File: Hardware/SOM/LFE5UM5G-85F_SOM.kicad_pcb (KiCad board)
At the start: 2 copper layers, 67.6 x 25.4 mm, 17 parts, among them J1 SODIMM-200_Split, U1 LFE5UM5G-85F-8BG381x, U2 AS4C256M16D3

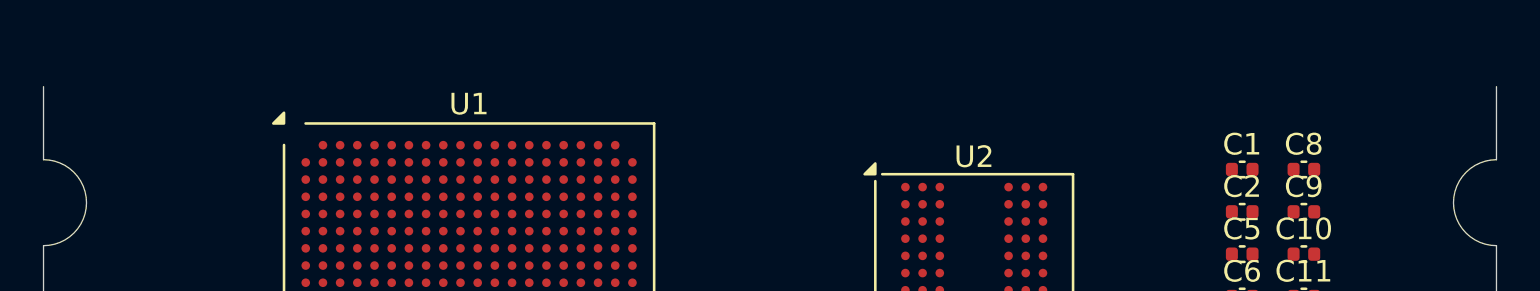
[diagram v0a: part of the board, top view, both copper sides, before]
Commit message: SOM board outline
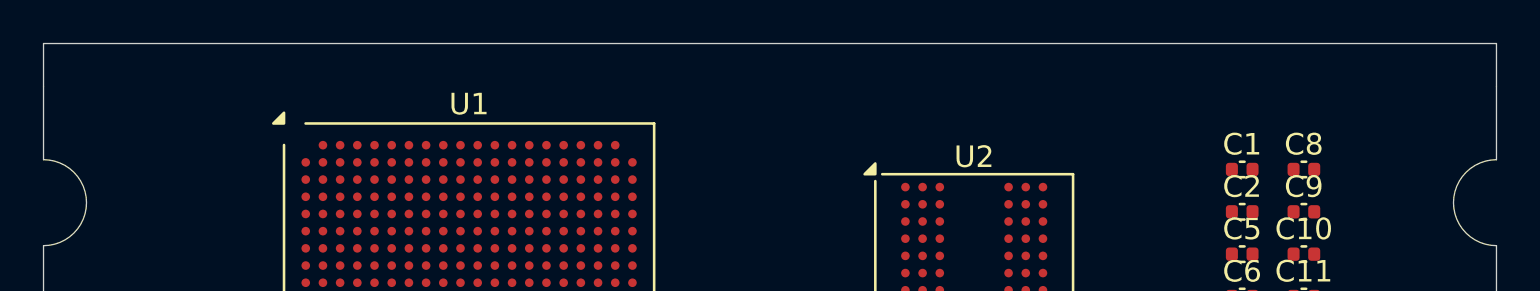
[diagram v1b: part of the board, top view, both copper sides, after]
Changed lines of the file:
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@@
+		)
+	)
+	(gr_line
+		(start 51.45 51.625)
+		(end 51.45 49.62)
+		(stroke
+			(width 0.05)
+			(type default)
+		)
+		(layer "Edge.Cuts")
+	)
+	(gr_line
+		(start 119.05 49.62)
+		(end 51.45 49.62)
+		(stroke
+			(width 0.05)
+			(type default)
+		)
+		(layer "Edge.Cuts")
+	)
+	(gr_line
+		(start 119.05 51.625)
+		(end 119.05 49.62)
+		(stroke
+			(width 0.05)
+			(type default)
+		)
+		(layer "Edge.Cuts")
+	)
+	(dimension
+		(type orthogonal)
+		(layer "F.Cu")
+		(pts
+			(xy 50.95 49.62) (xy 50.95 77.53)
+		)
+		(height -9.15)
+		(orientation 1)
+		(format
+			(prefix "")
+			(suffix "")
+			(units 3)
+			(units_format 1)
+			(precision 4)
+		)
+		(style
+			(thickness 0.2)
+			(arrow_length 1.27)
+			(text_position_mode 0)
+			(arrow_direction outward)
+			(extension_height 0.58642)
+			(extension_offset 0.5)
+			(keep_text_aligned yes)
+		)
+		(gr_text "27,9100 mm"
+			(at 40 63.575 90)
+			(layer "F.Cu")
+			(effects
+				(font
+					(size 1.5 1.5)
+					(thickness 0.3)
+				)
+			)
 		)
 	)

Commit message: BB SOM connector
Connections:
- J1 pad 2: unconnected-(J1-Pad2) -> ANY
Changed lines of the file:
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@@
 	(net 52 "unconnected-(J1-Pad55)")
 	(net 53 "unconnected-(J1-Pad152)")
-	(net 54 "unconnected-(J1-Pad2)")
+	(net 54 "ANY")
 	(net 55 "unconnected-(J1-Pad42)")
 	(net 56 "unconnected-(J1-Pad94)")
@@
 		)
 		(sheetname "/DDR/")
-		(sheetfile "ddr.kicad_sch")
+		(sheetfile "DDR.kicad_sch")
 		(attr smd)
 		(fp_line
@@
 		(property ki_fp_filters "Choke_* *Coil* Inductor_* L_*")
 		(sheetname "/DDR/")
-		(sheetfile "ddr.kicad_sch")
+		(sheetfile "DDR.kicad_sch")
 		(attr smd)
 		(fp_line
@@
 		)
 		(property ki_fp_filters "*SODIMM*")
-		(sheetname "/Connector/")
-		(sheetfile "connector.kicad_sch")
-		(attr exclude_from_pos_files allow_soldermask_bridges)
+		(sheetname "/SOM Connector/")
+		(sheetfile "Connector.kicad_sch")
+		(attr exclude_from_pos_files dnp allow_soldermask_bridges)
 		(fp_rect
 			(start -0.352 -1.302)
@@
 			(size 0.45 2.35)
 			(layers "B.Cu" "B.Mask")
-			(net 54 "unconnected-(J1-Pad2)")
+			(net 54 "ANY")
 			(pinfunction "2")
 			(pintype "passive")
@@
 		)
 		(sheetname "/DDR/")
-		(sheetfile "ddr.kicad_sch")
+		(sheetfile "DDR.kicad_sch")
 		(attr smd)
 		(fp_line
@@
 		)
 		(sheetname "/DDR/")
-		(sheetfile "ddr.kicad_sch")
+		(sheetfile "DDR.kicad_sch")
 		(attr smd)
 		(fp_line
@@
 		)
 		(sheetname "/DDR/")
-		(sheetfile "ddr.kicad_sch")
+		(sheetfile "DDR.kicad_sch")
 		(attr smd)
 		(fp_line
@@
 		)
 		(sheetname "/DDR/")
-		(sheetfile "ddr.kicad_sch")
+		(sheetfile "DDR.kicad_sch")
 		(attr smd)
 		(fp_line
@@
 		)
 		(sheetname "/DDR/")
-		(sheetfile "ddr.kicad_sch")
+		(sheetfile "DDR.kicad_sch")
 		(attr smd)
 		(fp_line
@@
 		)
 		(sheetname "/DDR/")
-		(sheetfile "ddr.kicad_sch")
+		(sheetfile "DDR.kicad_sch")
 		(attr smd)
 		(fp_line
@@
 		)
 		(sheetname "/DDR/")
-		(sheetfile "ddr.kicad_sch")
+		(sheetfile "DDR.kicad_sch")
 		(attr smd)
 		(fp_line
@@
 		(property ki_fp_filters "Lattice?caBGA*17x17mm*Layout20x20*P0.8mm*")
 		(sheetname "/FPGA/")
-		(sheetfile "io.kicad_sch")
+		(sheetfile "FPGA.kicad_sch")
 		(solder_mask_margin 0.075)
 		(attr smd)
@@
 		(property ki_fp_filters "Choke_* *Coil* Inductor_* L_*")
 		(sheetname "/DDR/")
-		(sheetfile "ddr.kicad_sch")
+		(sheetfile "DDR.kicad_sch")
 		(attr smd)
 		(fp_line
@@
 		)
 		(sheetname "/DDR/")
-		(sheetfile "ddr.kicad_sch")
+		(sheetfile "DDR.kicad_sch")
 		(attr smd)
 		(fp_line
@@
 		)
 		(sheetname "/DDR/")
-		(sheetfile "ddr.kicad_sch")
+		(sheetfile "DDR.kicad_sch")
 		(attr smd)
 		(fp_line
@@
 		)
 		(sheetname "/DDR/")
-		(sheetfile "ddr.kicad_sch")
+		(sheetfile "DDR.kicad_sch")
 		(attr smd)
 		(fp_line
@@
 		(property ki_fp_filters "BGA*9.0x13.0mm*P0.8mm*")
 		(sheetname "/DDR/")
-		(sheetfile "ddr.kicad_sch")
+		(sheetfile "DDR.kicad_sch")
 		(attr smd)
 		(fp_line
@@
 		)
 		(sheetname "/DDR/")
-		(sheetfile "ddr.kicad_sch")
+		(sheetfile "DDR.kicad_sch")
 		(attr smd)
 		(fp_line
@@
 		(layer "Edge.Cuts")
 	)
-	(dimension
-		(type orthogonal)
-		(layer "F.Cu")
-		(pts
-			(xy 50.95 49.62) (xy 50.95 77.53)
-		)
-		(height -9.15)
-		(orientation 1)
-		(format
-			(prefix "")
-			(suffix "")
-			(units 3)
-			(units_format 1)
-			(precision 4)
-		)
-		(style
-			(thickness 0.2)
-			(arrow_length 1.27)
-			(text_position_mode 0)
-			(arrow_direction outward)
-			(extension_height 0.58642)
-			(extension_offset 0.5)
-			(keep_text_aligned yes)
-		)
-		(gr_text "27,9100 mm"
-			(at 40 63.575 90)
-			(layer "F.Cu")
-			(effects
-				(font
-					(size 1.5 1.5)
-					(thickness 0.3)
-				)
-			)
-		)
-	)
 	(embedded_fonts no)

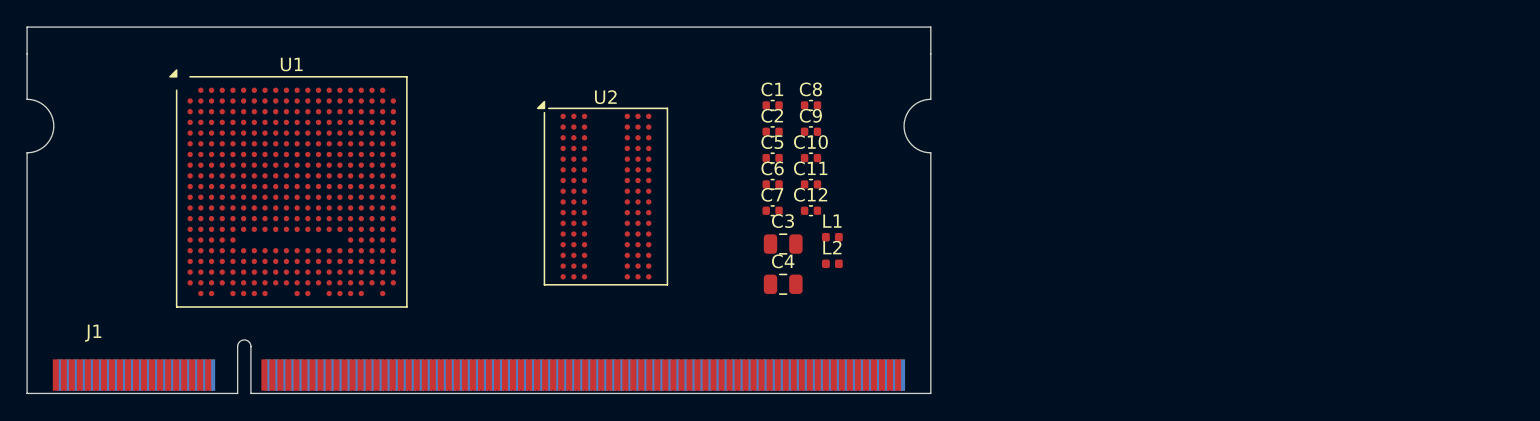
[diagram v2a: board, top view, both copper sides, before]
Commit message: SOM: DDR schematics update
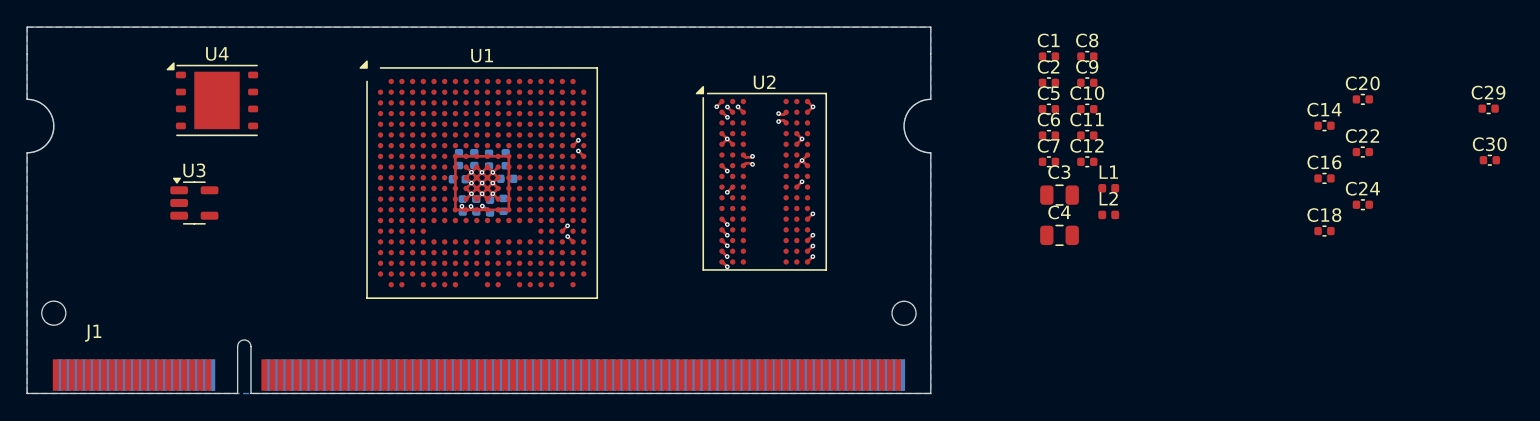
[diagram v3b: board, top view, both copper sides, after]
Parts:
- added C13: 100nF, Capacitor_SMD:C_0402_1005Metric, B.Cu at (84.0, 63.0)
- added C14: 100nF, Capacitor_SMD:C_0402_1005Metric, F.Cu at (148.5, 57.0)
- added C15: 100nF, Capacitor_SMD:C_0402_1005Metric, B.Cu at (85.1, 63.0)
- added C16: 100nF, Capacitor_SMD:C_0402_1005Metric, F.Cu at (148.5, 60.9)
- added C17: 100nF, Capacitor_SMD:C_0402_1005Metric, B.Cu at (86.1, 63.0)
- added C18: 10uF, Capacitor_SMD:C_0402_1005Metric, F.Cu at (148.5, 64.9)
- added C19: 100nF, Capacitor_SMD:C_0402_1005Metric, B.Cu at (87.1, 62.9)
- added C20: 100nF, Capacitor_SMD:C_0402_1005Metric, F.Cu at (151.4, 55.0)
- added C21: 100nF, Capacitor_SMD:C_0402_1005Metric, B.Cu at (87.2, 59.5)
- added C22: 100nF, Capacitor_SMD:C_0402_1005Metric, F.Cu at (151.4, 59.0)
- added C23: 100nF, Capacitor_SMD:C_0402_1005Metric, B.Cu at (86.0, 59.5)
- added C24: 10uF, Capacitor_SMD:C_0402_1005Metric, F.Cu at (151.4, 62.9)
- added C25: 100nF, Capacitor_SMD:C_0402_1005Metric, B.Cu at (84.9, 59.5)
- added C26: 100nF, Capacitor_SMD:C_0402_1005Metric, B.Cu at (83.8, 59.5)
- added C27: 100nF, Capacitor_SMD:C_0402_1005Metric, B.Cu at (83.8, 61.0)
- added C28: 100nF, Capacitor_SMD:C_0402_1005Metric, B.Cu at (87.4, 61.0)
- added C29: 10uF, Capacitor_SMD:C_0402_1005Metric, F.Cu at (160.8, 55.7)
- added C30: 10uF, Capacitor_SMD:C_0402_1005Metric, F.Cu at (160.9, 59.6)
- added U3: TLV62569DBV, Package_TO_SOT_SMD:SOT-23-5, F.Cu at (64.0, 62.8)
- added U4: W25Q128JVP, Package_SON:WSON-8-1EP_6x5mm_P1.27mm_EP3.4x4.3mm, F.Cu at (65.7, 55.1)
- U1: value LFE5UM5G-85F-8BG381x -> LFE5UM5G-85F
- moved L1 21.0 mm to (132.4, 61.7)
- moved L2 21.0 mm to (132.4, 63.7)
- moved C2 21.0 mm to (127.9, 53.8)
- moved C5 21.0 mm to (127.9, 55.8)
- moved C6 21.0 mm to (127.9, 57.7)
- moved C1 21.0 mm to (127.9, 51.8)
- moved C3 21.0 mm to (128.7, 62.2)
- moved C4 21.0 mm to (128.7, 65.2)
- moved C7 21.0 mm to (127.9, 59.7)
- moved C10 21.0 mm to (130.8, 55.8)
- moved C11 21.0 mm to (130.8, 57.7)
- moved C12 21.0 mm to (130.8, 59.7)
- moved C8 21.0 mm to (130.8, 51.8)
- moved C9 21.0 mm to (130.8, 53.8)
- moved U1 14.3 mm to (85.5, 61.3)
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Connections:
- net Net-(U1A-VCC-PadH10) renamed VCC_CORE
- U1 pad C20: unconnected-(U1D-PR35A-PadC20) -> DDR_DQ8
- U1 pad D19: unconnected-(U1D-PR35B-PadD19) -> DDR_DQ9
- U1 pad D20: unconnected-(U1D-PR35C-PadD20) -> DDR_DQ10
- U1 pad E19: unconnected-(U1D-PR35D-PadE19) -> DDR_DQ11
- U1 pad E20: unconnected-(U1D-PR38A-PadE20) -> DDR_DQ12
- U1 pad F19: unconnected-(U1D-PR38B-PadF19) -> DDR_DQ13
- U1 pad F20: unconnected-(U1D-PR38C-PadF20) -> DDR_DQ14
- U1 pad G19: unconnected-(U1D-PR41A-PadG19) -> DDR_UDQS_N
- U1 pad G20: unconnected-(U1D-PR38D-PadG20) -> DDR_DQ15
- U1 pad H14: Net-(U1D-VCCIO2-PadH14) -> 1.5V
- U1 pad H15: Net-(U1D-VCCIO2-PadH14) -> 1.5V
- U1 pad H20: unconnected-(U1D-PR41B-PadH20) -> DDR_UDQS_P
- U1 pad J15: Net-(U1D-VCCIO2-PadH14) -> 1.5V
- U1 pad L14: Net-(U1E-VCCIO3-PadL14) -> 1.5V
- U1 pad L15: Net-(U1E-VCCIO3-PadL14) -> 1.5V
- U1 pad M15: Net-(U1E-VCCIO3-PadL14) -> 1.5V
- U1 pad N19: unconnected-(U1E-PR83A-PadN19) -> DDR_DQ0
- U1 pad N20: unconnected-(U1E-PR83B-PadN20) -> DDR_DQ1
- U1 pad P18: unconnected-(U1E-PR83D-PadP18) -> DDR_DQ3
- U1 pad P19: unconnected-(U1E-PR83C-PadP19) -> DDR_DQ2
- U1 pad P20: unconnected-(U1E-PR86A-PadP20) -> DDR_DQ4
- U1 pad R18: unconnected-(U1E-PR89B-PadR18) -> DDR_LDQS_P
- U1 pad R20: unconnected-(U1E-PR86B-PadR20) -> DDR_DQ5
- U1 pad R5: unconnected-(U1I-TDI-PadR5) -> JTAG_TDI
- U1 pad T19: unconnected-(U1E-PR89A-PadT19) -> DDR_LDQS_N
- U1 pad T20: unconnected-(U1E-PR86C-PadT20) -> DDR_DQ6
- U1 pad T5: unconnected-(U1I-TCK-PadT5) -> JTAG_TCK
- U1 pad U20: unconnected-(U1E-PR86D-PadU20) -> DDR_DQ7
- U1 pad U5: unconnected-(U1I-TMS-PadU5) -> JTAG_TMS
- U1 pad V4: unconnected-(U1I-TDO-PadV4) -> JTAG_TDO
- U2 pad B7: DDR_NUDQS -> DDR_UDQS_N
- U2 pad C7: DDR_UDQS -> DDR_UDQS_P
- U2 pad F3: DDR_LDQS -> DDR_LDQS_P
- U2 pad G3: DDR_NLDQS -> DDR_LDQS_N
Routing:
- net Net-(U1A-GND-PadB14): track 0.00 -> 20.4 mm, vias 0 -> 9
- net DDR_UDQS_P: track 0.00 -> 19.3 mm, vias 0 -> 2
- net DDR_UDQS_N: track 0.00 -> 19.3 mm, vias 0 -> 2
- net VCC_CORE: track 0.00 -> 18.9 mm, vias 0 -> 3
- net DDR_LDQS_P: track 0.00 -> 17.5 mm, vias 0 -> 2
- net DDR_LDQS_N: track 0.00 -> 17.5 mm, vias 0 -> 2
- net GND: track 0.00 -> 11.9 mm, vias 0 -> 15
- net DDR_VDD_1.5V: track 0.00 -> 2.25 mm, vias 0 -> 4
- net DDR_VDDQ_1.5V: track 0.00 -> 0.55 mm, vias 0 -> 1
- added copper zone on B.Cu, net GND
- added copper zone on In1.Cu, net GND
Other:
- copper layers 2 -> 6

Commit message: SOM layout fix
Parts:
- added C31: 100nF, Capacitor_SMD:C_0402_1005Metric, F.Cu at (150.1, 45.0)
- added C32: 100nF, Capacitor_SMD:C_0402_1005Metric, F.Cu at (150.1, 47.0)
- added C33: 10uF, Capacitor_SMD:C_0402_1005Metric, F.Cu at (150.1, 48.9)
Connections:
- U1 pad A15: unconnected-(U1C-PT103A-PadA15) -> DDR_A1
- U1 pad A16: unconnected-(U1C-PT110A-PadA16) -> DDR_A6
- U1 pad A17: unconnected-(U1C-PT116A-PadA17) -> DDR_A12
- U1 pad A18: unconnected-(U1C-PT119A-PadA18) -> DDR_A14
- U1 pad A19: unconnected-(U1C-PT121A-PadA19) -> DDR_BA1
- U1 pad B15: unconnected-(U1C-PT105A-PadB15) -> DDR_A2
- U1 pad B16: unconnected-(U1C-PT110B-PadB16) -> DDR_A7
- U1 pad B17: unconnected-(U1C-PT114A-PadB17) -> DDR_A10
- U1 pad B18: unconnected-(U1C-PT116B-PadB18) -> DDR_A13
- U1 pad B19: unconnected-(U1C-PT119B-PadB19) -> DDR_BA0
- U1 pad B20: unconnected-(U1C-PT121B-PadB20) -> DDR_BA2
- U1 pad C15: unconnected-(U1C-PT105B-PadC15) -> DDR_A3
- U1 pad C16: unconnected-(U1C-PT112A-PadC16) -> DDR_A8
- U1 pad C17: unconnected-(U1C-PT114B-PadC17) -> DDR_A11
- U1 pad D15: unconnected-(U1C-PT107A-PadD15) -> DDR_A4
- U1 pad D16: unconnected-(U1C-PT112B-PadD16) -> DDR_A9
- U1 pad E14: unconnected-(U1C-PT85B-PadE14) -> DDR_A0
- U1 pad E15: unconnected-(U1C-PT107B-PadE15) -> DDR_A5
- U1 pad G19: DDR_UDQS_N -> DDR_UDQS_P
- U1 pad H20: DDR_UDQS_P -> DDR_UDQS_N
- U1 pad R18: DDR_LDQS_P -> DDR_LDQS_N
- U1 pad T19: DDR_LDQS_N -> DDR_LDQS_P
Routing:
- net DDR_UDQS_P: track 19.3 -> 1.23 mm
- net DDR_UDQS_N: track 19.3 -> 1.23 mm
- net DDR_LDQS_P: track 17.5 -> 1.36 mm
- net DDR_LDQS_N: track 17.5 -> 1.35 mm

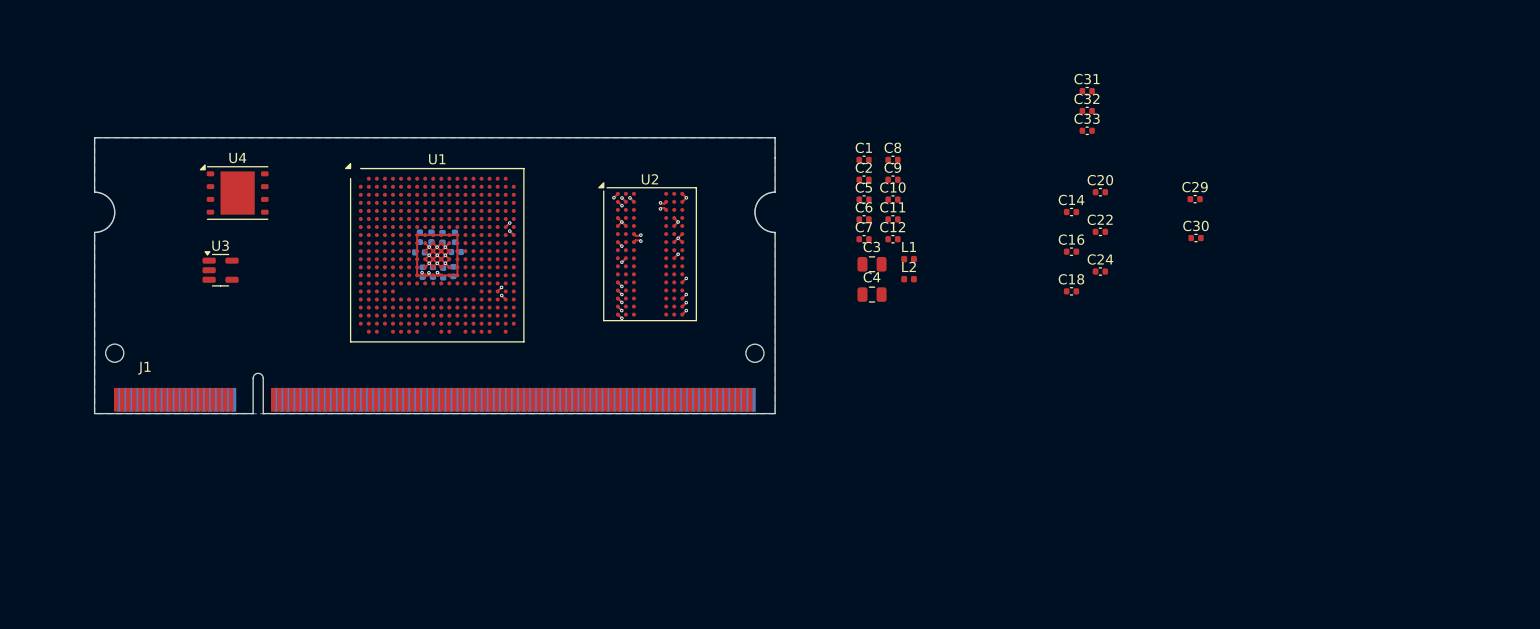
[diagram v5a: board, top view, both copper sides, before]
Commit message: PCIe M.2 connector changed
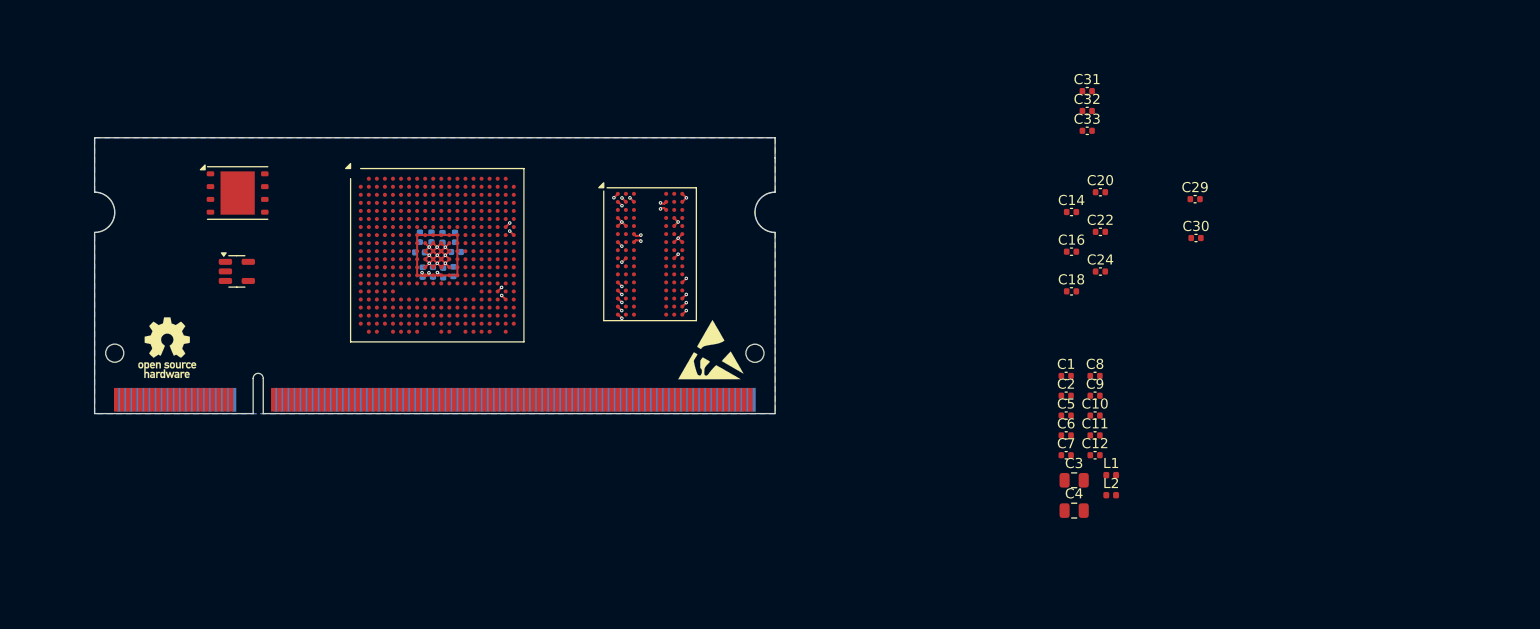
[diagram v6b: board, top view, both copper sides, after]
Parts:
- added REF**: OSHW-Logo_5.7x6mm_SilkScreen, Symbol:OSHW-Logo_5.7x6mm_SilkScreen, F.Cu at (58.7, 70.5)
- added REF**: ESD-Logo_6.6x6mm_SilkScreen, Symbol:ESD-Logo_6.6x6mm_SilkScreen, F.Cu at (112.7, 70.7)
- moved C10 29.4 mm to (150.8, 77.2)
- moved C11 29.4 mm to (150.8, 79.2)
- moved C8 29.4 mm to (150.8, 73.3)
- moved C9 29.4 mm to (150.8, 75.2)
- moved C1 29.4 mm to (148.0, 73.3)
- moved C12 29.4 mm to (150.8, 81.2)
- moved C2 29.4 mm to (148.0, 75.2)
- moved C5 29.4 mm to (148.0, 77.2)
- moved C6 29.4 mm to (148.0, 79.2)
- moved C3 29.4 mm to (148.8, 83.7)
- moved C7 29.4 mm to (148.0, 81.2)
- moved C4 29.4 mm to (148.8, 86.7)
- moved L1 29.4 mm to (152.4, 83.1)
- moved L2 29.4 mm to (152.4, 85.1)
- moved U3 1.62 mm to (65.6, 62.9)
